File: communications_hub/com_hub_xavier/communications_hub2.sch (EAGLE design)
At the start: 49 parts, among them CON1 SM04B-GHS-TB, CON2 SM04B-GHS-TB, CON3 SM02B-GHS-TB, CON6 UAVCAN_MICRO, CON7 UAVCAN_MICRO, Q1 DMN5L06K, Q2 DMN5L06K, U1 TCAN1042HVDR, U2 TCAN1042HVDR

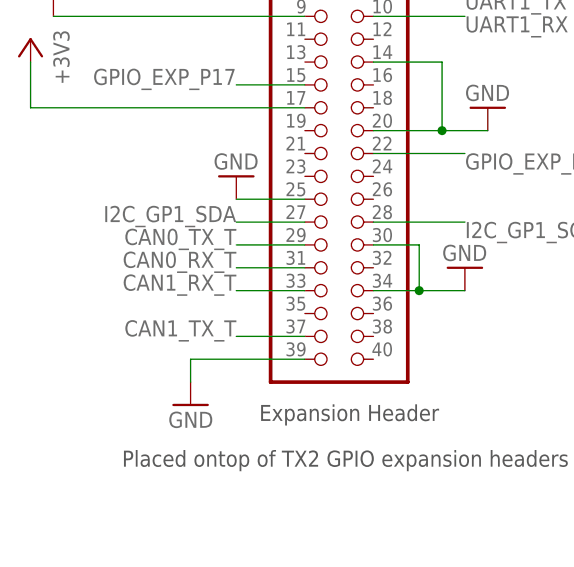
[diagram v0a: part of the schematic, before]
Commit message: Extra traces are removed, gound plane is added. Default DRC is passed. Info of the board is added as well.
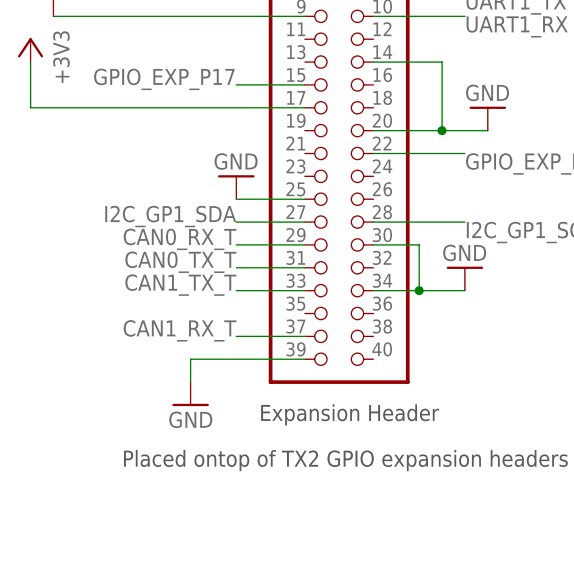
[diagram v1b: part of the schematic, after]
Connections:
- net CAN0_RX_T: now also JP21.29; no longer JP21.31
- net CAN0_TX_T: now also JP21.31; no longer JP21.29
- net CAN1_RX_T: now also JP21.37; no longer JP21.33
- net CAN1_TX_T: now also JP21.33; no longer JP21.37
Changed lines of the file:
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@@
 <net name="CAN0_RX_T" class="0">
-<segment>
-<pinref part="JP21" gate="A" pin="31"/>
-<wire x1="-71.12" y1="17.78" x2="-78.74" y2="17.78" width="0.1524" layer="91"/>
-<label x="-78.74" y="17.78" size="1.778" layer="95" rot="MR0"/>
-</segment>
 <segment>
 <pinref part="R2" gate="G$1" pin="1"/>
@@
 <label x="0" y="99.06" size="1.778" layer="95" rot="MR0" xref="yes"/>
 </segment>
+<segment>
+<pinref part="JP21" gate="A" pin="29"/>
+<wire x1="-71.12" y1="20.32" x2="-78.74" y2="20.32" width="0.1524" layer="91"/>
+<label x="-78.74" y="20.32" size="1.778" layer="95" rot="MR0"/>
+</segment>
 </net>
 <net name="CAN1_TX_T" class="0">
+<segment>
+<pinref part="R4" gate="G$1" pin="1"/>
+<wire x1="2.54" y1="66.04" x2="0" y2="66.04" width="0.1524" layer="91"/>
+<label x="0" y="66.04" size="1.778" layer="95" rot="MR0" xref="yes"/>
+</segment>
+<segment>
+<pinref part="JP21" gate="A" pin="33"/>
+<wire x1="-71.12" y1="15.24" x2="-78.74" y2="15.24" width="0.1524" layer="91"/>
+<label x="-78.74" y="15.24" size="1.778" layer="95" rot="MR0"/>
+</segment>
+</net>
+<net name="CAN1_RX_T" class="0">
+<segment>
+<pinref part="R5" gate="G$1" pin="1"/>
+<wire x1="2.54" y1="58.42" x2="0" y2="58.42" width="0.1524" layer="91"/>
+<label x="0" y="58.42" size="1.778" layer="95" rot="MR0" xref="yes"/>
+</segment>
 <segment>
 <pinref part="JP21" gate="A" pin="37"/>
 <wire x1="-71.12" y1="10.16" x2="-78.74" y2="10.16" width="0.1524" layer="91"/>
 <label x="-78.74" y="10.16" size="1.778" layer="95" rot="MR0"/>
-</segment>
-<segment>
-<pinref part="R4" gate="G$1" pin="1"/>
-<wire x1="2.54" y1="66.04" x2="0" y2="66.04" width="0.1524" layer="91"/>
-<label x="0" y="66.04" size="1.778" layer="95" rot="MR0" xref="yes"/>
-</segment>
-</net>
-<net name="CAN1_RX_T" class="0">
-<segment>
-<pinref part="JP21" gate="A" pin="33"/>
-<wire x1="-71.12" y1="15.24" x2="-78.74" y2="15.24" width="0.1524" layer="91"/>
-<label x="-78.74" y="15.24" size="1.778" layer="95" rot="MR0"/>
-</segment>
-<segment>
-<pinref part="R5" gate="G$1" pin="1"/>
-<wire x1="2.54" y1="58.42" x2="0" y2="58.42" width="0.1524" layer="91"/>
-<label x="0" y="58.42" size="1.778" layer="95" rot="MR0" xref="yes"/>
 </segment>
 </net>
@@
 <net name="CAN0_TX_T" class="0">
 <segment>
-<pinref part="JP21" gate="A" pin="29"/>
-<wire x1="-71.12" y1="20.32" x2="-78.74" y2="20.32" width="0.1524" layer="91"/>
-<label x="-78.74" y="20.32" size="1.778" layer="95" rot="MR0"/>
-</segment>
-<segment>
 <pinref part="R1" gate="G$1" pin="1"/>
 <wire x1="2.54" y1="106.68" x2="0" y2="106.68" width="0.1524" layer="91"/>
 <label x="0" y="106.68" size="1.778" layer="95" rot="MR0" xref="yes"/>
 </segment>
-</net>
+<segment>
+<pinref part="JP21" gate="A" pin="31"/>
+<wire x1="-71.12" y1="17.78" x2="-78.74" y2="17.78" width="0.1524" layer="91"/>
+<label x="-78.74" y="17.78" size="1.778" layer="95" rot="MR0"/>
+</segment>
+</net>

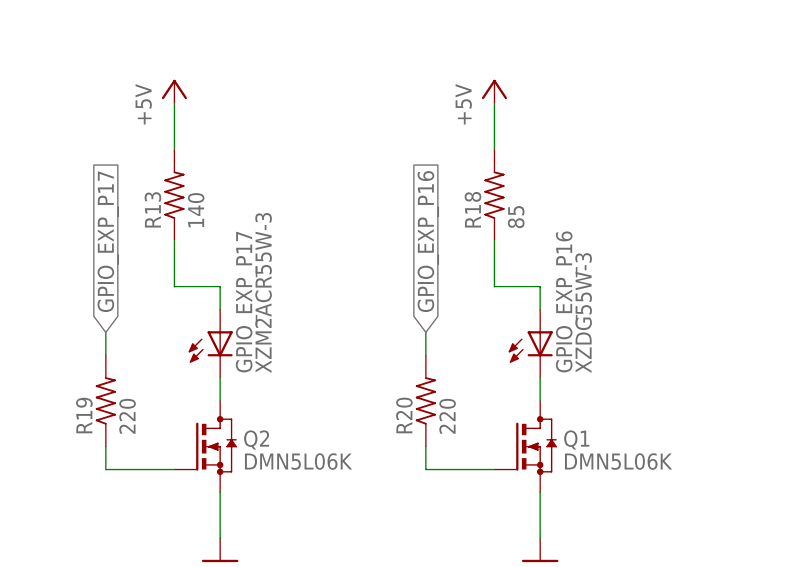
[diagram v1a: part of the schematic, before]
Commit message: Routed a couple airwires thrown in the DRC, modified some silkscreen. Project still requires BOM.
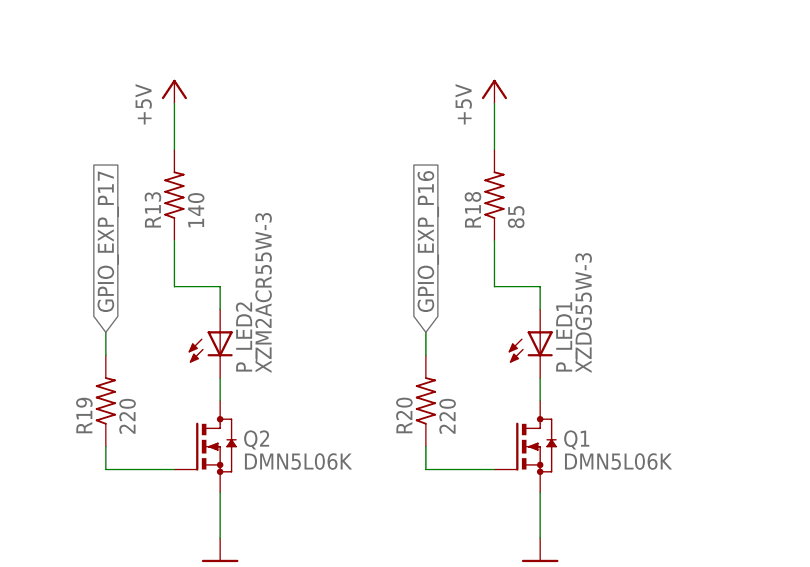
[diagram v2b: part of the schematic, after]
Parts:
- renumbered GPIO_EXP_P16 to P_LED1, GPIO_EXP_P17 to P_LED2
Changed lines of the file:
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@@
 <?xml version="1.0" encoding="utf-8"?>
 <!DOCTYPE eagle SYSTEM "eagle.dtd">
-<eagle version="9.4.0">
+<eagle version="9.2.2">
 <drawing>
 <settings>
@@
 <part name="R11" library="resistor" library_urn="urn:adsk.eagle:library:348" deviceset="R-US_" device="M1206" package3d_urn="urn:adsk.eagle:package:23566/1" value="10K"/>
 <part name="+3V311" library="supply1" library_urn="urn:adsk.eagle:library:371" deviceset="+3V3" device=""/>
-<part name="GPIO_EXP_P17" library="eagle-ltspice" library_urn="urn:adsk.eagle:library:217" deviceset="LED_E" device="" package3d_urn="urn:adsk.eagle:package:13319/1" value="XZM2ACR55W-3"/>
-<part name="GPIO_EXP_P16" library="eagle-ltspice" library_urn="urn:adsk.eagle:library:217" deviceset="LED_E" device="" package3d_urn="urn:adsk.eagle:package:13319/1" value="XZDG55W-3"/>
+<part name="P_LED2" library="eagle-ltspice" library_urn="urn:adsk.eagle:library:217" deviceset="LED_E" device="" package3d_urn="urn:adsk.eagle:package:13319/1" value="XZM2ACR55W-3"/>
+<part name="P_LED1" library="eagle-ltspice" library_urn="urn:adsk.eagle:library:217" deviceset="LED_E" device="" package3d_urn="urn:adsk.eagle:package:13319/1" value="XZDG55W-3"/>
 <part name="GND21" library="supply1" library_urn="urn:adsk.eagle:library:371" deviceset="GND" device=""/>
 <part name="GND22" library="supply1" library_urn="urn:adsk.eagle:library:371" deviceset="GND" device=""/>
@@
 <attribute name="VALUE" x="43.18" y="2.54" size="1.778" layer="96" rot="R90"/>
 </instance>
-<instance part="GPIO_EXP_P17" gate="G$1" x="86.36" y="0" smashed="yes">
+<instance part="P_LED2" gate="G$1" x="86.36" y="0" smashed="yes">
 <attribute name="NAME" x="89.916" y="-4.572" size="1.778" layer="95" rot="R90"/>
 <attribute name="VALUE" x="92.075" y="-4.572" size="1.778" layer="96" rot="R90"/>
 </instance>
-<instance part="GPIO_EXP_P16" gate="G$1" x="121.92" y="0" smashed="yes">
+<instance part="P_LED1" gate="G$1" x="121.92" y="0" smashed="yes">
 <attribute name="NAME" x="125.476" y="-4.572" size="1.778" layer="95" rot="R90"/>
 <attribute name="VALUE" x="127.635" y="-4.572" size="1.778" layer="96" rot="R90"/>
@@
 <net name="N$3" class="0">
 <segment>
-<pinref part="GPIO_EXP_P17" gate="G$1" pin="A"/>
+<pinref part="P_LED2" gate="G$1" pin="A"/>
 <pinref part="R13" gate="G$1" pin="1"/>
 <wire x1="86.36" y1="2.54" x2="86.36" y2="5.08" width="0.1524" layer="91"/>
@@
 <net name="N$4" class="0">
 <segment>
-<pinref part="GPIO_EXP_P16" gate="G$1" pin="A"/>
+<pinref part="P_LED1" gate="G$1" pin="A"/>
 <pinref part="R18" gate="G$1" pin="1"/>
 <wire x1="121.92" y1="2.54" x2="121.92" y2="5.08" width="0.1524" layer="91"/>
@@
 <net name="N$9" class="0">
 <segment>
-<pinref part="GPIO_EXP_P17" gate="G$1" pin="C"/>
+<pinref part="P_LED2" gate="G$1" pin="C"/>
 <pinref part="Q2" gate="G$1" pin="D"/>
 <wire x1="86.36" y1="-5.08" x2="86.36" y2="-7.62" width="0.1524" layer="91"/>
@@
 <net name="N$10" class="0">
 <segment>
-<pinref part="GPIO_EXP_P16" gate="G$1" pin="C"/>
+<pinref part="P_LED1" gate="G$1" pin="C"/>
 <pinref part="Q1" gate="G$1" pin="D"/>
 <wire x1="121.92" y1="-5.08" x2="121.92" y2="-7.62" width="0.1524" layer="91"/>

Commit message: Added a pullup resistor to pin 18 of JP21 for the Go switch. Made slight edits to the BOM to clean up formatting.
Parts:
- added R23: 4.7k, audio amplifier example:R-US_R0603
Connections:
- new net N$1: JP21.18, R23.1
- net +3V3: now also R23.2
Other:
- note added: "Pull up resistor for GO Switch"
- note added: "When the Go switch is screwed all the way in, pin 18 on JP21 is pulled to GND. Under normal circumstances the Go switch will be screwed in all the way. To start the Jetson Xavier, the Go switch will have to be unscrewed, which will open circuit the path to ground and allow R23 to pull the line high. The '1' on the line will be read by software and will cause the Jetson to start."
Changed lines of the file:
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@@
 <layer number="115" name="ReferenceISLANDS" color="7" fill="1" visible="yes" active="yes"/>
 <layer number="116" name="Patch_BOT" color="9" fill="4" visible="yes" active="yes"/>
+<layer number="117" name="BACKMAAT1" color="7" fill="1" visible="yes" active="yes"/>
 <layer number="118" name="Rect_Pads" color="7" fill="1" visible="yes" active="yes"/>
+<layer number="119" name="KAP_TEKEN" color="7" fill="1" visible="yes" active="yes"/>
+<layer number="120" name="KAP_MAAT1" color="7" fill="1" visible="yes" active="yes"/>
 <layer number="121" name="sName" color="7" fill="1" visible="yes" active="yes"/>
 <layer number="122" name="_bPlace" color="7" fill="1" visible="yes" active="yes"/>
@@
 <layer number="128" name="_bValues" color="7" fill="1" visible="yes" active="yes"/>
 <layer number="129" name="Mask" color="7" fill="1" visible="yes" active="yes"/>
+<layer number="130" name="SMDSTROOK" color="7" fill="1" visible="yes" active="yes"/>
 <layer number="131" name="tAdjust" color="7" fill="1" visible="no" active="yes"/>
 <layer number="132" name="bAdjust" color="7" fill="1" visible="no" active="yes"/>
+<layer number="133" name="bottom_silk" color="7" fill="1" visible="yes" active="yes"/>
+<layer number="134" name="silk_top" color="7" fill="1" visible="yes" active="yes"/>
+<layer number="135" name="silk_bottom" color="7" fill="1" visible="yes" active="yes"/>
+<layer number="136" name="silktop" color="7" fill="1" visible="yes" active="yes"/>
+<layer number="137" name="silkbottom" color="7" fill="1" visible="yes" active="yes"/>
 <layer number="144" name="Drill_legend" color="7" fill="1" visible="yes" active="yes"/>
+<layer number="145" name="DrillLegend_01-16" color="7" fill="1" visible="yes" active="yes"/>
+<layer number="146" name="DrillLegend_01-20" color="7" fill="1" visible="yes" active="yes"/>
 <layer number="150" name="Notes" color="7" fill="1" visible="no" active="yes"/>
 <layer number="151" name="HeatSink" color="7" fill="1" visible="yes" active="yes"/>
@@
 <layer number="154" name="FabDoc2" color="2" fill="1" visible="no" active="no"/>
 <layer number="155" name="FabDoc3" color="7" fill="15" visible="no" active="no"/>
+<layer number="166" name="AntennaArea" color="7" fill="1" visible="yes" active="yes"/>
+<layer number="168" name="4mmHeightArea" color="7" fill="1" visible="yes" active="yes"/>
 <layer number="199" name="Contour" color="7" fill="1" visible="yes" active="yes"/>
 <layer number="200" name="200bmp" color="1" fill="10" visible="yes" active="yes"/>
@@
 <part name="CON6" library="SPEAR-general" deviceset="UAVCAN_MICRO" device=""/>
 <part name="CON7" library="SPEAR-general" deviceset="UAVCAN_MICRO" device=""/>
+<part name="R23" library="audio amplifier example" library_urn="urn:adsk.eagle:library:970892" deviceset="R-US_" device="R0603" package3d_urn="urn:adsk.eagle:package:970938/2" value="4.7k"/>
+<part name="+3V3" library="supply1" library_urn="urn:adsk.eagle:library:371" deviceset="+3V3" device=""/>
 </parts>
 <sheets>
@@
 Amber LED for +3v3
 ~2V for amber, 1.3V / 20mA = 65R</text>
+<text x="-53.34" y="40.64" size="1.778" layer="91">Pull up resistor for GO Switch</text>
+<text x="-86.36" y="71.12" size="1.778" layer="91"> When the Go switch is screwed all the
+ way in, pin 18 on JP21 is pulled to GND.
+ Under normal circumstances the Go
+ switch will be screwed in all the way. To
+ start the Jetson Xavier, the Go switch
+ will have to be unscrewed, which will
+ open circuit the path to ground and
+ allow R23 to pull the line high. The '1'
+ on the line will be read by software and
+ will cause the Jetson to start.</text>
 </plain>
 <instances>
@@
 <attribute name="VALUE" x="-45.72" y="55.88" size="1.778" layer="96" rot="MR180"/>
 </instance>
-<instance part="GND8" gate="1" x="-50.8" y="35.56" smashed="yes" rot="MR180">
-<attribute name="VALUE" x="-53.34" y="38.1" size="1.778" layer="96" rot="MR180"/>
+<instance part="GND8" gate="1" x="-48.26" y="33.02" smashed="yes" rot="MR270">
+<attribute name="VALUE" x="-45.72" y="35.56" size="1.778" layer="96" rot="MR270"/>
 </instance>
 <instance part="GND2" gate="1" x="-83.82" y="2.54" smashed="yes" rot="MR0">
@@
 <attribute name="VALUE" x="-81.28" y="30.48" size="1.778" layer="96" rot="MR180"/>
 </instance>
-<instance part="GND6" gate="1" x="-53.34" y="17.78" smashed="yes" rot="MR180">
-<attribute name="VALUE" x="-55.88" y="20.32" size="1.778" layer="96" rot="MR180"/>
+<instance part="GND6" gate="1" x="-55.88" y="12.7" smashed="yes" rot="MR0">
+<attribute name="VALUE" x="-53.34" y="10.16" size="1.778" layer="96" rot="MR0"/>
 </instance>
 <instance part="+3V31" gate="G$1" x="-101.6" y="43.18" smashed="yes" rot="MR0">
@@
 <instance part="CON6" gate="G$1" x="157.48" y="99.06" smashed="yes" rot="MR0"/>
 <instance part="CON7" gate="G$1" x="170.18" y="58.42" smashed="yes" rot="MR0"/>
+<instance part="R23" gate="G$1" x="-40.64" y="38.1" smashed="yes">
+<attribute name="NAME" x="-38.862" y="34.7726" size="1.778" layer="95"/>
+<attribute name="VALUE" x="-44.45" y="34.798" size="1.778" layer="96"/>
+</instance>
+<instance part="+3V3" gate="G$1" x="-17.78" y="40.64" smashed="yes" rot="MR0">
+<attribute name="VALUE" x="-15.24" y="35.56" size="1.778" layer="96" rot="MR90"/>
+</instance>
 </instances>
 <busses>
@@
 <wire x1="-58.42" y1="20.32" x2="-58.42" y2="15.24" width="0.1524" layer="91"/>
 <pinref part="GND6" gate="1" pin="GND"/>
-<wire x1="-58.42" y1="15.24" x2="-53.34" y2="15.24" width="0.1524" layer="91"/>
+<wire x1="-58.42" y1="15.24" x2="-55.88" y2="15.24" width="0.1524" layer="91"/>
 <pinref part="JP21" gate="A" pin="34"/>
 <wire x1="-63.5" y1="15.24" x2="-58.42" y2="15.24" width="0.1524" layer="91"/>
@@
 <pinref part="R3" gate="G$1" pin="1"/>
 <wire x1="-12.7" y1="91.44" x2="2.54" y2="91.44" width="0.1524" layer="91"/>
+</segment>
+<segment>
+<pinref part="R23" gate="G$1" pin="2"/>
+<wire x1="-35.56" y1="38.1" x2="-17.78" y2="38.1" width="0.1524" layer="91"/>
+<pinref part="+3V3" gate="G$1" pin="+3V3"/>
 </segment>
 </net>
@@
 </segment>
 </net>
+<net name="N$1" class="0">
+<segment>
+<pinref part="JP21" gate="A" pin="18"/>
+<wire x1="-63.5" y1="35.56" x2="-58.42" y2="35.56" width="0.1524" layer="91"/>
+<wire x1="-58.42" y1="35.56" x2="-58.42" y2="38.1" width="0.1524" layer="91"/>
+<wire x1="-58.42" y1="38.1" x2="-45.72" y2="38.1" width="0.1524" layer="91"/>
+<pinref part="R23" gate="G$1" pin="1"/>
+</segment>
+</net>
